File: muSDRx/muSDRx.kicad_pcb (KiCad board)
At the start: 2 copper layers, 100 x 100 mm, 98 parts, among them CON1 SJ1-3523N, CON2 SJ1-3523N, J1 Conn_01x02_Male, J11 Conn_01x02_Male, J2 Conn_01x02_Male, J3 Conn_01x02_Male, J4 Conn_01x02_Male, J5 Conn_01x02_Male, J6 Conn_01x02_Male, J9 Conn_01x04_Male, P1 BNC, Q1 MMBT2222A-TP, SW1 SW_Push, SW2 SW_Push, SW3 Rotary_Encoder_Switch, U1 LCD1602, U2 Si5351A-B-GT, U3 SN74CBT3253, U4 BluePill, U5 LT6231 (or LM4562), U6 MC78M05_TO252, Y1 CX3225

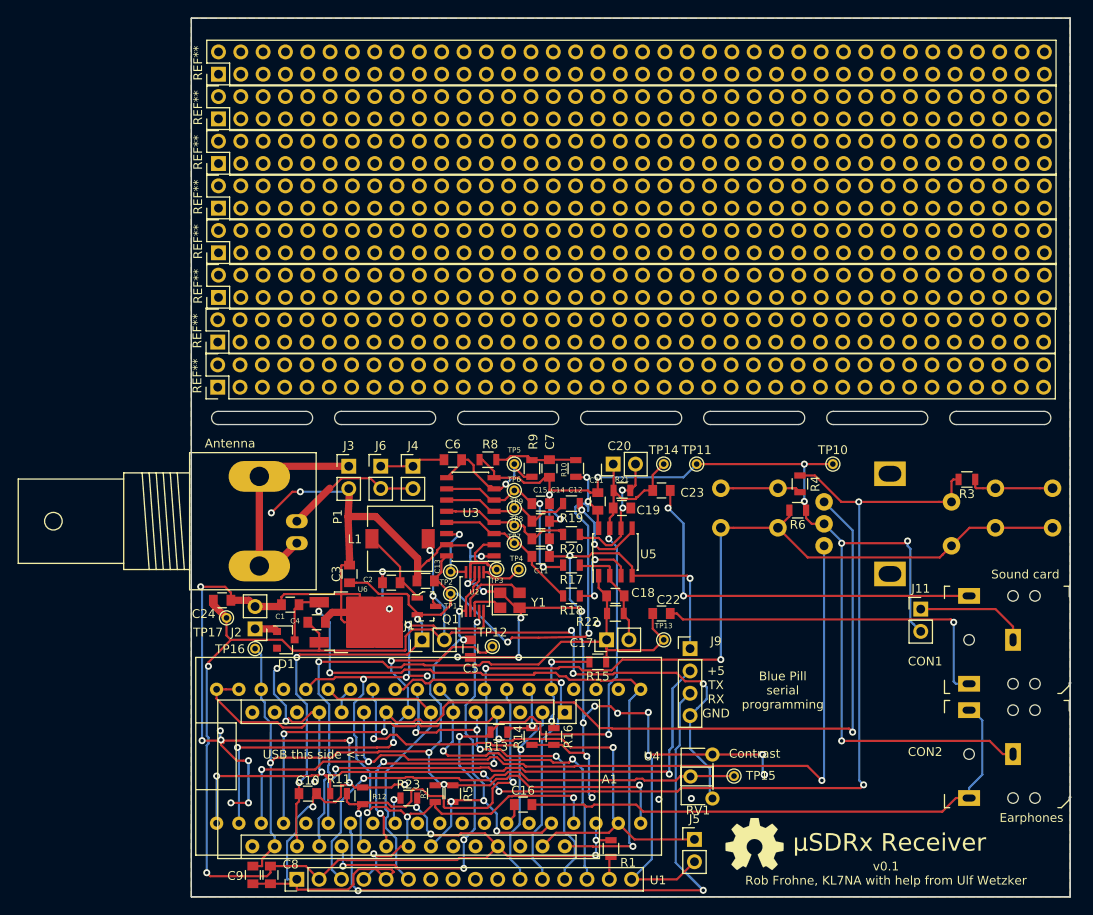
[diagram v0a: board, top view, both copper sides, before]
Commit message: Rerouted analog section
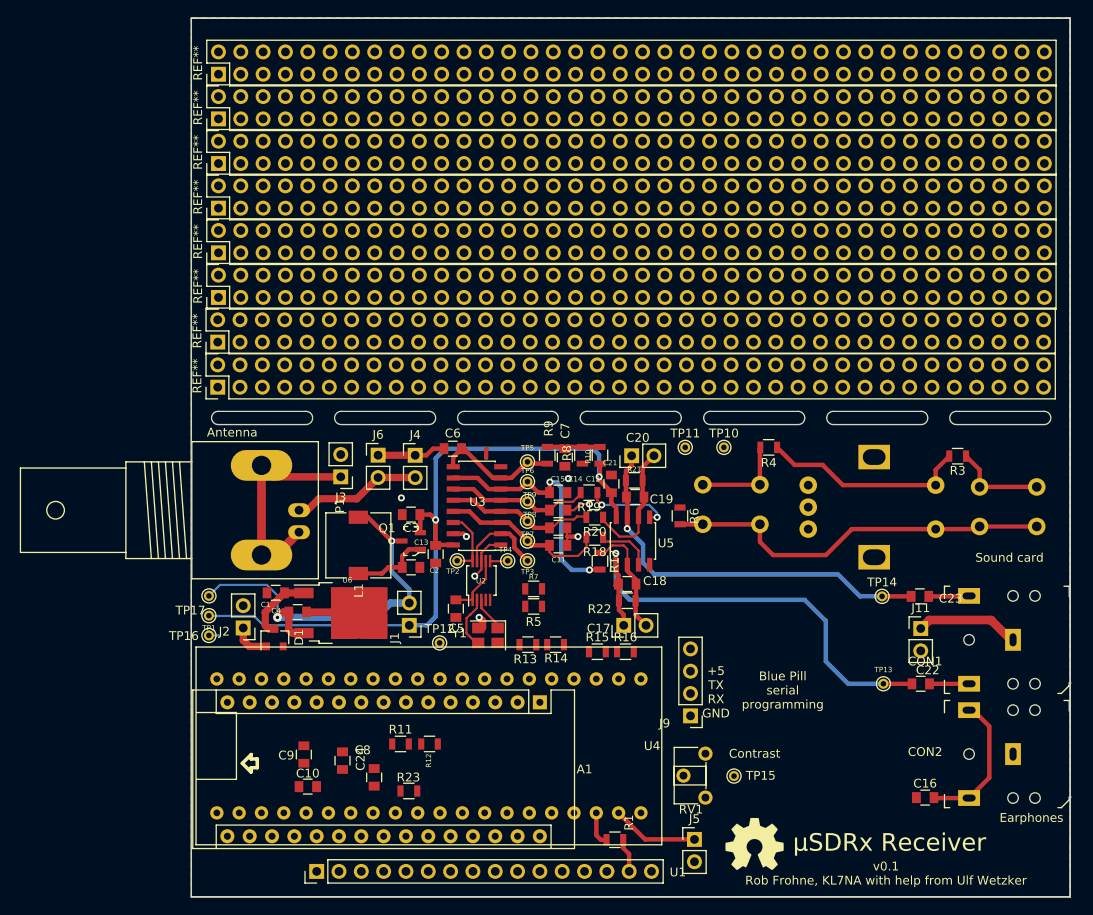
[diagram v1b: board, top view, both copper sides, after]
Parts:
- moved C16 45.8 mm to (133.5, 138.7)
- moved C23 31.8 mm to (132.9, 115.8)
- moved C22 30.6 mm to (133.0, 125.8)
- moved TP14 29.1 mm to (128.6, 115.8)
- moved TP1 27.6 mm to (52.0, 118.0)
- moved C24 26.6 mm to (70.8, 136.4), turned to 270 degrees
- moved R7 25.9 mm to (89.0, 115.0), turned to 0 degrees
- moved TP13 25.5 mm to (128.8, 125.8)
- moved R5 23.2 mm to (89.0, 117.0), turned to 0 degrees
- moved C8 15.4 mm to (67.2, 134.5)
- moved C9 14.9 mm to (62.8, 133.8)
- moved R6 13.4 mm to (105.6, 106.7), turned to 270 degrees
- moved R16 12.6 mm to (99.4, 122.1), turned to 0 degrees
- moved TP10 12.5 mm to (110.6, 98.8)
- moved R14 10.8 mm to (91.5, 121.3), turned to 0 degrees
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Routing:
- net GND: track 473.6 -> 22.9 mm, vias 48 -> 7
- net +5V: track 195.3 -> 50.3 mm, vias 11 -> 2
- net /VHI: track 156.1 -> 23.8 mm, vias 8 -> 0
- net /ROT_B: track 108.1 -> 0.00 mm, vias 3 -> 0
- net /ROT_A: track 104.7 -> 0.00 mm, vias 3 -> 0
- net +3V3: track 106.5 -> 8.17 mm, vias 6 -> 0
- net /RS: track 89.4 -> 0.00 mm, vias 8 -> 0
- net /BUTTON: track 120.2 -> 44.8 mm, vias 5 -> 0
- net Net-(J9-Pad3): track 74.8 -> 0.00 mm, vias 2 -> 0
- net Net-(A1-Pad29): track 83.1 -> 9.88 mm, vias 2 -> 0
- net /V_IN: track 78.8 -> 8.09 mm, vias 3 -> 0
- net Net-(RV1-Pad2): track 58.1 -> 0.00 mm, vias 1 -> 0
- net /SIG_OUT: track 57.9 -> 0.00 mm, vias 2 -> 0
- net /FREQ_COUNT: track 50.2 -> 0.00 mm, vias 3 -> 0
- net /AUD_1: track 92.8 -> 45.4 mm, vias 6 -> 1
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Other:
- board text removed: "USB this side <--"
- board text removed: "µSDRx Receiver, v0.1 After µSDX, by PE1NNZ Rob Frohne KL7NA with help from Ulf Wetzker"

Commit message: Rerouted digital section
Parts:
- U1: moved to B.Cu
- moved C24 26.6 mm to (97.3, 137.9), turned to 0 degrees
- moved R12 17.9 mm to (59.2, 133.4), turned to 180 degrees
- moved C8 16.2 mm to (83.1, 137.7), turned to 0 degrees
- moved R11 12.2 mm to (61.7, 131.4), turned to 270 degrees
- moved C10 8.70 mm to (60.2, 145.6)
- moved R16 8.50 mm to (92.8, 127.5)
- moved J9 7.60 mm to (106.8, 121.8), turned to 0 degrees
- moved C9 6.13 mm to (57.2, 136.4), turned to 0 degrees
- moved R14 5.86 mm to (85.8, 122.8), turned to 180 degrees
- moved R15 5.15 mm to (91.0, 122.2), turned to 270 degrees
- moved R5 3.18 mm to (87.5, 114.1)
- moved J1 2.55 mm to (74.8, 116.5), turned to 0 degrees
- moved R23 2.45 mm to (72.3, 138.1), turned to 0 degrees
- moved TP17 2.39 mm to (52.8, 118.0)
- moved TP1 2.37 mm to (52.8, 115.8)
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- renumbered REF** to REF1, REF** to REF2, REF** to REF3, REF** to REF4, REF** to REF5, REF** to REF6, REF** to REF7, REF** to REF8
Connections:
- C16 pad 1: Net-(C16-Pad1) -> (no net)
- C22 pad 1: Net-(C22-Pad1) -> (no net)
- C23 pad 1: Net-(C23-Pad1) -> (no net)
- J3 pad 1: Net-(J3-Pad1) -> (no net)
- R18 pad 1: Net-(R18-Pad1) -> (no net)
- R19 pad 1: Net-(R19-Pad1) -> (no net)
- U2 pad 2: Net-(U2-Pad2) -> (no net)
- U2 pad 3: Net-(U2-Pad3) -> (no net)
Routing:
- net +5V: track 50.3 -> 178.1 mm, vias 2 -> 3
- net /VHI: track 23.8 -> 146.4 mm
- net /ROT_A: track 0.00 -> 103.1 mm
- net /AUD_1: track 45.4 -> 143.6 mm, vias 1 -> 3
- net /RS: track 0.00 -> 97.4 mm, vias 0 -> 1
- net +3V3: track 8.17 -> 100.1 mm, vias 0 -> 1
- net /ROT_B: track 0.00 -> 90.2 mm
- net /AUD_0: track 53.3 -> 142.5 mm, vias 1 -> 3
- net /BUTTON: track 44.8 -> 122.5 mm
- net Net-(A1-Pad29): track 9.88 -> 82.6 mm, vias 0 -> 1
- net /V_IN: track 8.09 -> 77.4 mm, vias 0 -> 2
- net /D4: track 0.00 -> 59.7 mm, vias 0 -> 1
- net /SCL: track 0.00 -> 52.2 mm, vias 0 -> 1
- net Net-(RV1-Pad2): track 0.00 -> 50.7 mm
- net Net-(C16-Pad2): track 0.00 -> 48.8 mm
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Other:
- board text added: "USB Port"
